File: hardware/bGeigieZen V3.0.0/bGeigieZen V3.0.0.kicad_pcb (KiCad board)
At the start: 2 copper layers, 129.4 x 64.6 mm, 17 parts, among them J1 M5 2x15 pin, J10 QI GND, J11 QI charger Plus, J2 Geiger IRover, J3 GPS, J4 Geiger Safepulse, J5 Extra support header, J6 Grove, J8 QI charger ground, J9 QI Plus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

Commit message: Updated Board V3.0.0
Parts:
- moved J6 3.77 mm to (158.4, 120.2)
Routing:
- net 3.3V: track 140.5 -> 132.3 mm, vias 1 -> 0
- net /SDA: track 49.1 -> 43.4 mm, vias 1 -> 0
- net Net-(BT1--): track 59.1 -> 64.5 mm
- net /SCL: track 50.5 -> 52.4 mm

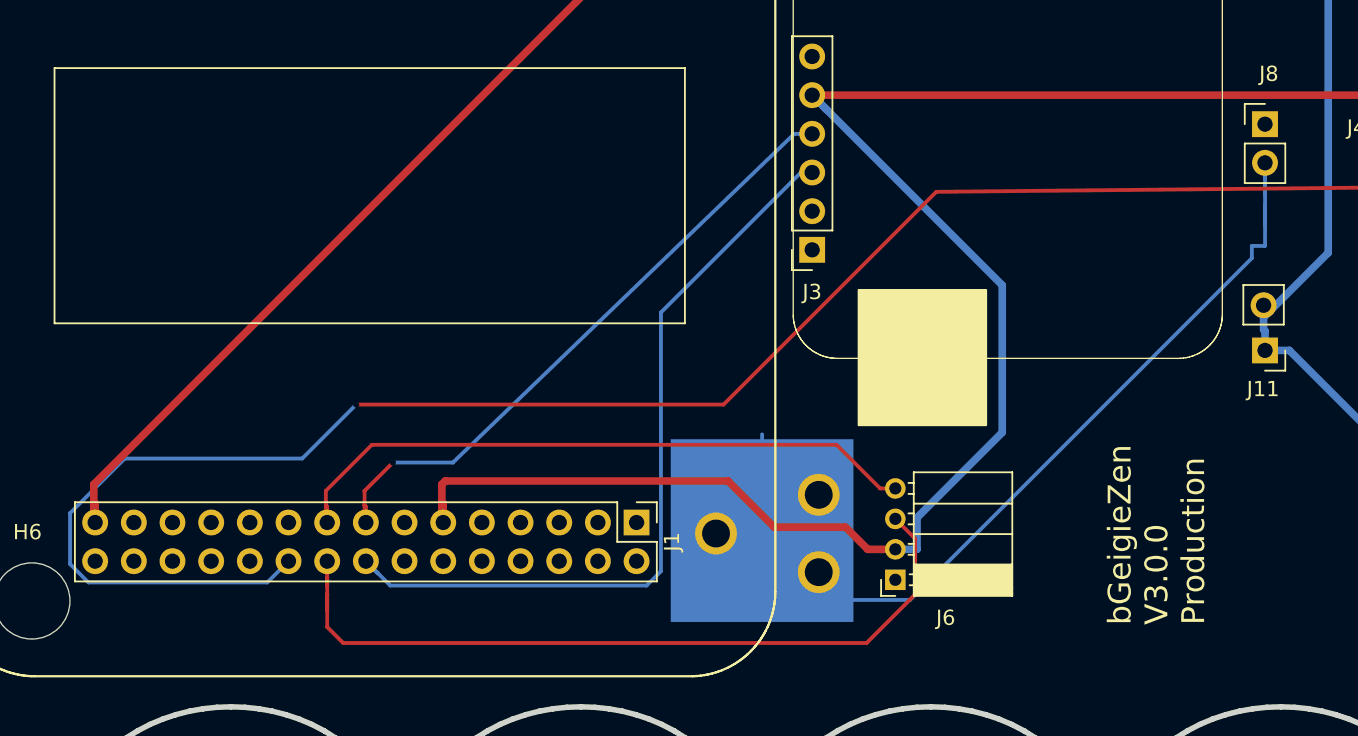
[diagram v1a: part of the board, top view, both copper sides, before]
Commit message: Updated board for IMU and I2C
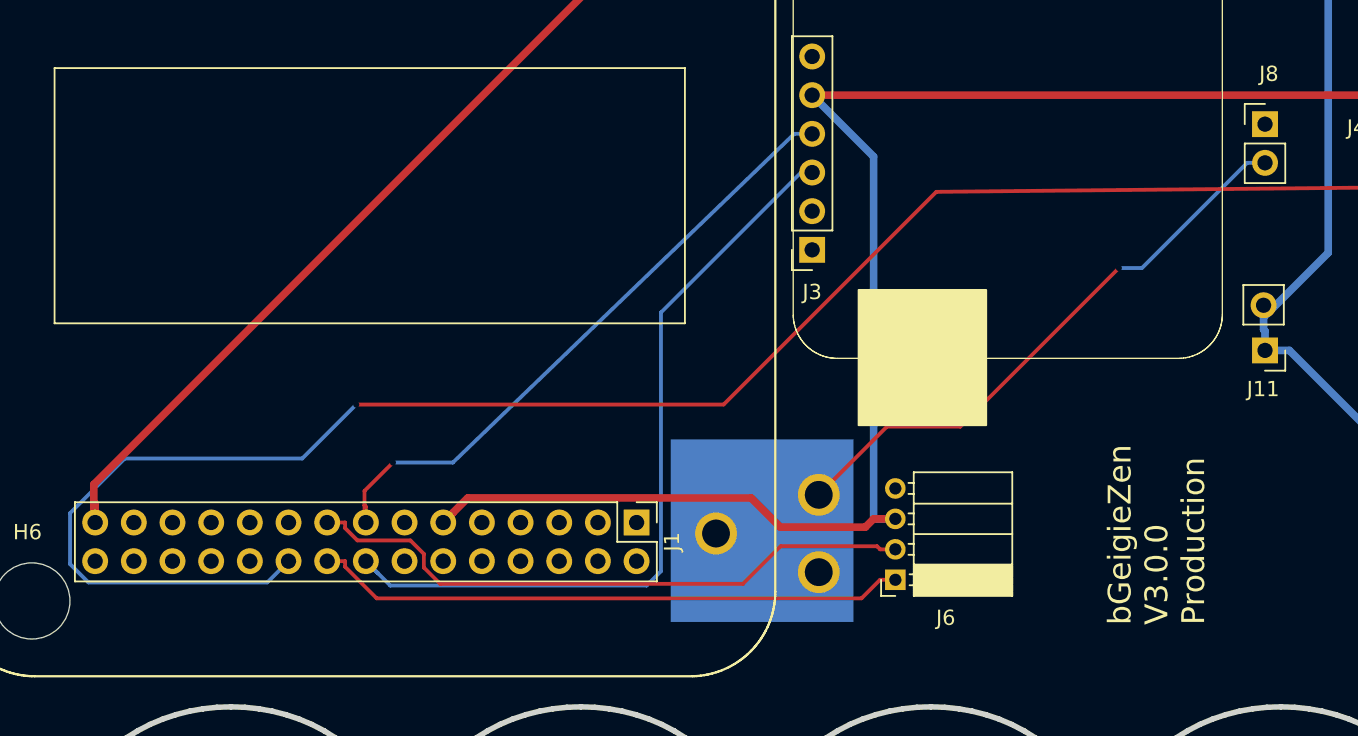
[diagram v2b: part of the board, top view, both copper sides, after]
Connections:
- J6 pad 1: GND -> /SCL
- J6 pad 2: 3.3V -> /SDA
- J6 pad 3: /SCL -> 3.3V
- J6 pad 4: /SDA -> GND
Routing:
- net Net-(BT1--): track 64.5 -> 49.9 mm, vias 0 -> 1
- net /SCL: track 52.4 -> 39.0 mm
- net 3.3V: track 132.3 -> 119.3 mm
- net /SDA: track 43.4 -> 40.8 mm
- net /GIO2 on Core and GIO32 on Core-2: track 138.0 -> 137.1 mm

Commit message: Created n gerbers for V3..0. production boards.
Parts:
- added Logo: LOGO, bGeigieRaku_M5_1015:18650 map, B.Cu at (177.9, 117.3)
- J8: value QI charger ground -> LiPo ground
- moved J6 39.1 mm to (197.1, 114.4), turned to 0 degrees
- moved G back 5.23 mm to (90.9, 99.8)
- moved J3 2.42 mm to (152.9, 96.1)
- moved SW1 1.93 mm to (183.0, 72.6)
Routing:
- net /SCL: track 39.0 -> 81.6 mm
- net /SDA: track 40.8 -> 77.4 mm
- net /GIO2 on Core and GIO32 on Core-2: track 137.1 -> 106.0 mm, vias 1 -> 0
- net 3.3V: track 119.3 -> 131.2 mm
- net /VBATT: track 66.4 -> 67.9 mm
- net /RX2: track 42.4 -> 44.0 mm
- net /TX2: track 51.9 -> 53.1 mm
- net /BAT: track 96.5 -> 95.4 mm
- net Net-(BT1--): track 49.9 -> 49.8 mm, vias 1 -> 0
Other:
- board text added: "-"
- board text added: "IRover"

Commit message: Updated V3.0.0 boards
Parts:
- moved J10 0.94 mm to (209.8, 91.4)
- moved J8 0.94 mm to (182.5, 91.2)
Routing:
- net Net-(J9-Pin_1): track 2.54 -> 0.00 mm
- net Net-(BT1--): track 49.8 -> 48.8 mm

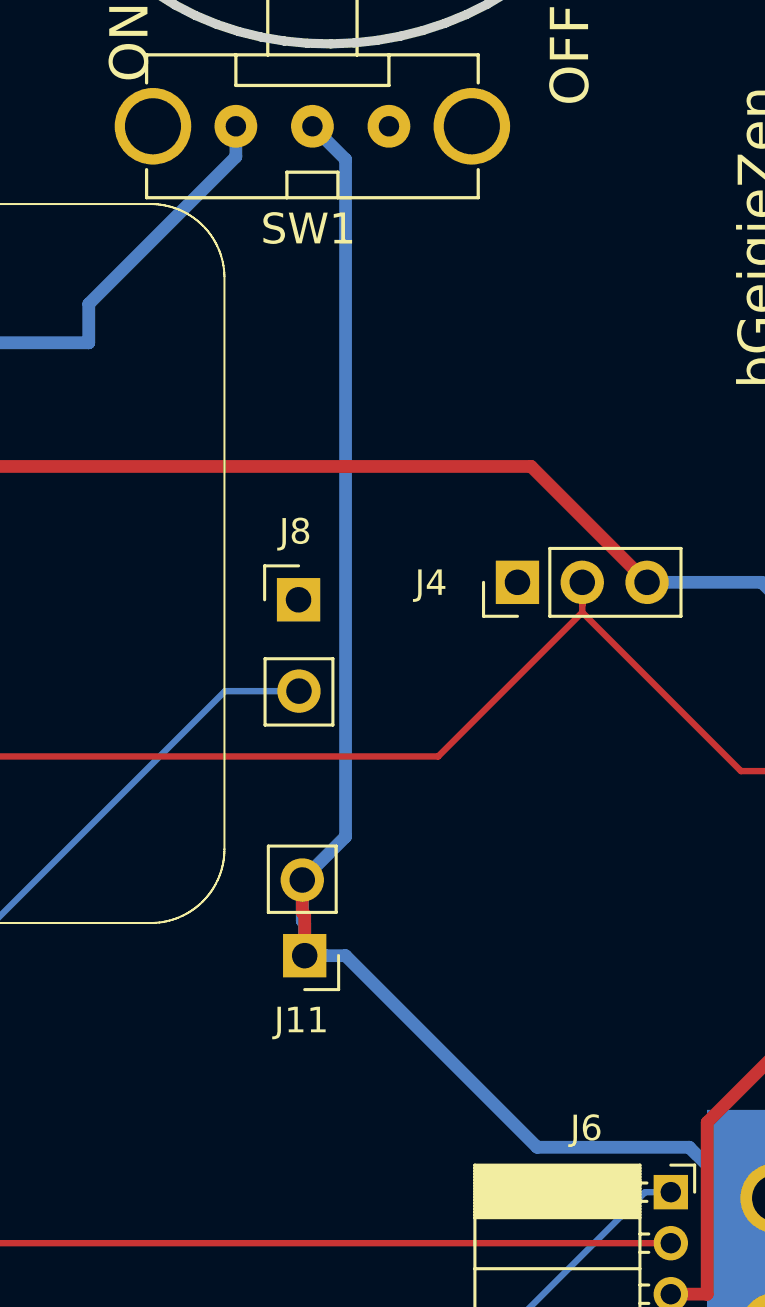
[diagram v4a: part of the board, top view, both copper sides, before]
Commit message: Updated 4056 placement
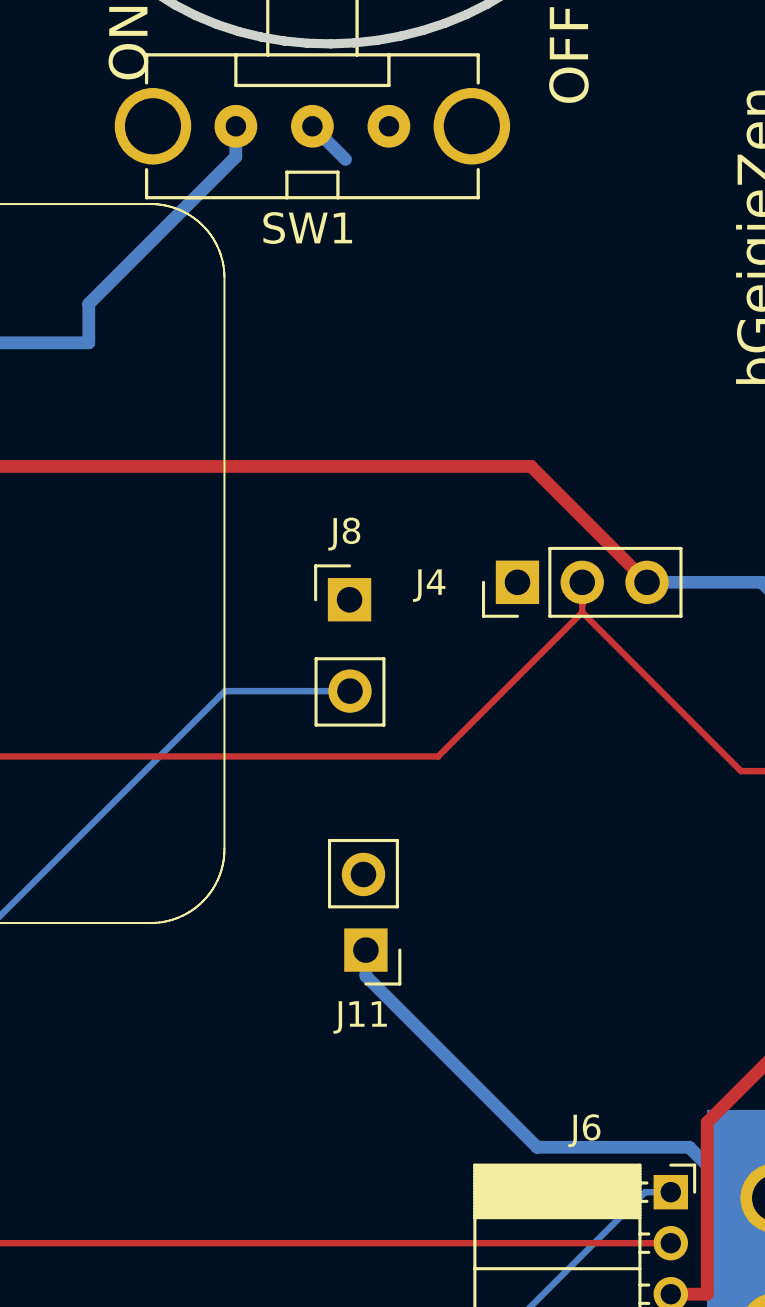
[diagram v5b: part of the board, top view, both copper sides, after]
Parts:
- moved J11 2.41 mm to (185.1, 104.9)
- moved J8 2.00 mm to (184.5, 91.2)
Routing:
- net /VBATT: track 67.9 -> 31.3 mm
- net Net-(BT1--): track 48.8 -> 50.8 mm
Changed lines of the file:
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@@
   )
   (footprint "bGeigieZen:PinHeader_1x02_P2.54mm_Vertical_4056" (layer "F.Cu")
-    (at 182.7276 105.104 180)
+    (at 185.127021 104.8856 180)
     (descr "Through hole straight pin header, 1x02, 2.54mm pitch, single row")
     (tags "Through hole pin header THT 1x02 2.54mm single row")
@@
   )
   (footprint "Connector_PinHeader_2.54mm:PinHeader_1x02_P2.54mm_Vertical" (layer "F.Cu")
-    (at 182.486504 91.153824)
+    (at 184.486504 91.153824)
     (descr "Through hole straight pin header, 1x02, 2.54mm pitch, single row")
     (tags "Through hole pin header THT 1x02 2.54mm single row")
@@
   (segment (start 128.7526 113.2324) (end 128.7526 116.407) (width 0.5) (layer "B.Cu") (net 4))
   (segment (start 152.883 85.9274) (end 152.883 85.9272) (width 0.5) (layer "B.Cu") (net 4))
-  (segment (start 182.632 103.407) (end 182.728 103.502) (width 0.5) (layer "F.Cu") (net 7))
-  (segment (start 182.632 102.138) (end 182.632 102.1385) (width 0.5) (layer "F.Cu") (net 7))
-  (segment (start 182.728 103.502) (end 182.728 104.303) (width 0.5) (layer "F.Cu") (net 7))
-  (segment (start 182.632 102.1385) (end 182.632 103.407) (width 0.5) (layer "F.Cu") (net 7))
+  (segment (start 191.839 112.614) (end 185.127021 105.902021) (width 0.5) (layer "B.Cu") (net 7))
   (segment (start 200.711 117.15) (end 198.78 115.219) (width 0.5) (layer "B.Cu") (net 7))
   (segment (start 207.926 117.15) (end 207.9256 117.15) (width 0.5) (layer "B.Cu") (net 7))
-  (segment (start 182.728 103.836) (end 182.632 103.74) (width 0.5) (layer "B.Cu") (net 7))
-  (segment (start 183.5285 105.104) (end 182.7276 105.104) (width 0.5) (layer "B.Cu") (net 7))
   (segment (start 204.4976 117.15) (end 200.711 117.15) (width 0.5) (layer "B.Cu") (net 7))
-  (segment (start 182.632 102.138) (end 184.3293 100.4407) (width 0.5) (layer "B.Cu") (net 7))
   (segment (start 184.3293 73.8917) (end 183.0296 72.592) (width 0.5) (layer "B.Cu") (net 7))
   (segment (start 198.78 113.592) (end 197.801 112.614) (width 0.5) (layer "B.Cu") (net 7))
-  (segment (start 184.3293 100.4407) (end 184.3293 73.8917) (width 0.5) (layer "B.Cu") (net 7))
-  (segment (start 182.728 105.104) (end 182.728 103.836) (width 0.5) (layer "B.Cu") (net 7))
   (segment (start 198.78 115.219) (end 198.78 113.592) (width 0.5) (layer "B.Cu") (net 7))
-  (segment (start 184.329 105.104) (end 183.5285 105.104) (width 0.5) (layer "B.Cu") (net 7))
   (segment (start 207.9256 117.15) (end 204.4976 117.15) (width 0.5) (layer "B.Cu") (net 7))
   (segment (start 197.801 112.614) (end 191.839 112.614) (width 0.5) (layer "B.Cu") (net 7))
-  (segment (start 183.5285 105.104) (end 182.728 105.104) (width 0.5) (layer "B.Cu") (net 7))
-  (segment (start 182.632 103.74) (end 182.632 102.1385) (width 0.5) (layer "B.Cu") (net 7))
-  (segment (start 182.632 102.138) (end 182.632 102.1385) (width 0.5) (layer "B.Cu") (net 7))
-  (segment (start 191.839 112.614) (end 184.329 105.104) (width 0.5) (layer "B.Cu") (net 7))
+  (segment (start 185.127021 105.902021) (end 185.127021 104.8856) (width 0.5) (layer "B.Cu") (net 7))
   (segment (start 207.108 97.87) (end 199.831 97.87) (width 0.25) (layer "F.Cu") (net 19))
   (segment (start 193.6076 90.7637) (end 193.6076 90.47) (width 0.25) (layer "F.Cu") (net 19))
@@
   (segment (start 149.6976 116.9404) (end 149.698 116.94) (width 0.25) (layer "B.Cu") (net 34))
   (segment (start 153.418 114.59) (end 159.746 114.59) (width 0.25) (layer "B.Cu") (net 34))
-  (segment (start 179.601868 94.734132) (end 182.502811 94.734132) (width 0.25) (layer "B.Cu") (net 34))
   (segment (start 146.67 117.13) (end 149.508 117.13) (width 0.25) (layer "B.Cu") (net 34))
   (segment (start 153.4176 114.5904) (end 153.418 114.59) (width 0.25) (layer "B.Cu") (net 34))
@@
   (segment (start 151.068 117.32) (end 153.4176 119.6696) (width 0.25) (layer "B.Cu") (net 34))
   (segment (start 153.4176 114.5904) (end 153.4176 114.59) (width 0.25) (layer "B.Cu") (net 34))
+  (segment (start 179.601868 94.734132) (end 184.502811 94.734132) (width 0.25) (layer "B.Cu") (net 34))
   (zone (net 1) (net_name "GND") (layers "F&B.Cu") (name "GND") (hatch edge 0.508)
     (connect_pads (clearance 0.508))

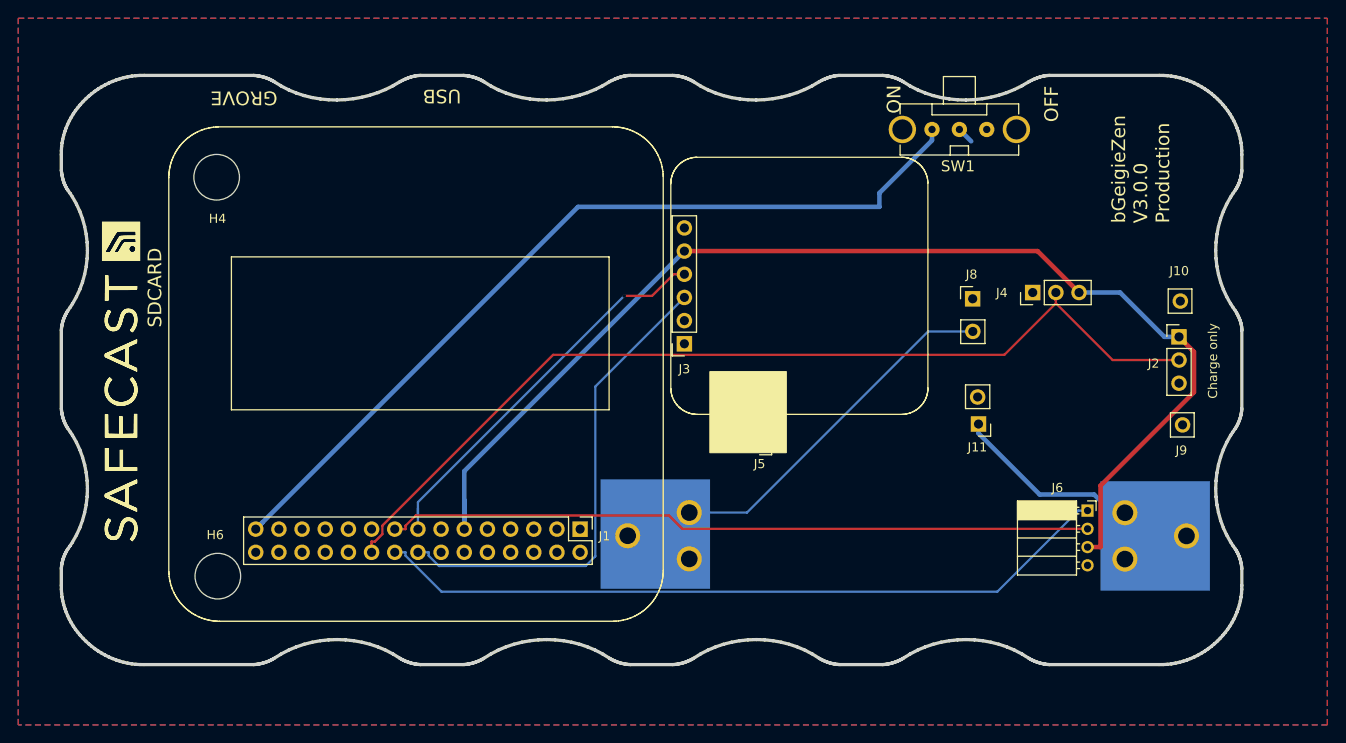
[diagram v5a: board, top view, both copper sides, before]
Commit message: Updated Grove connector on board V3.0.1
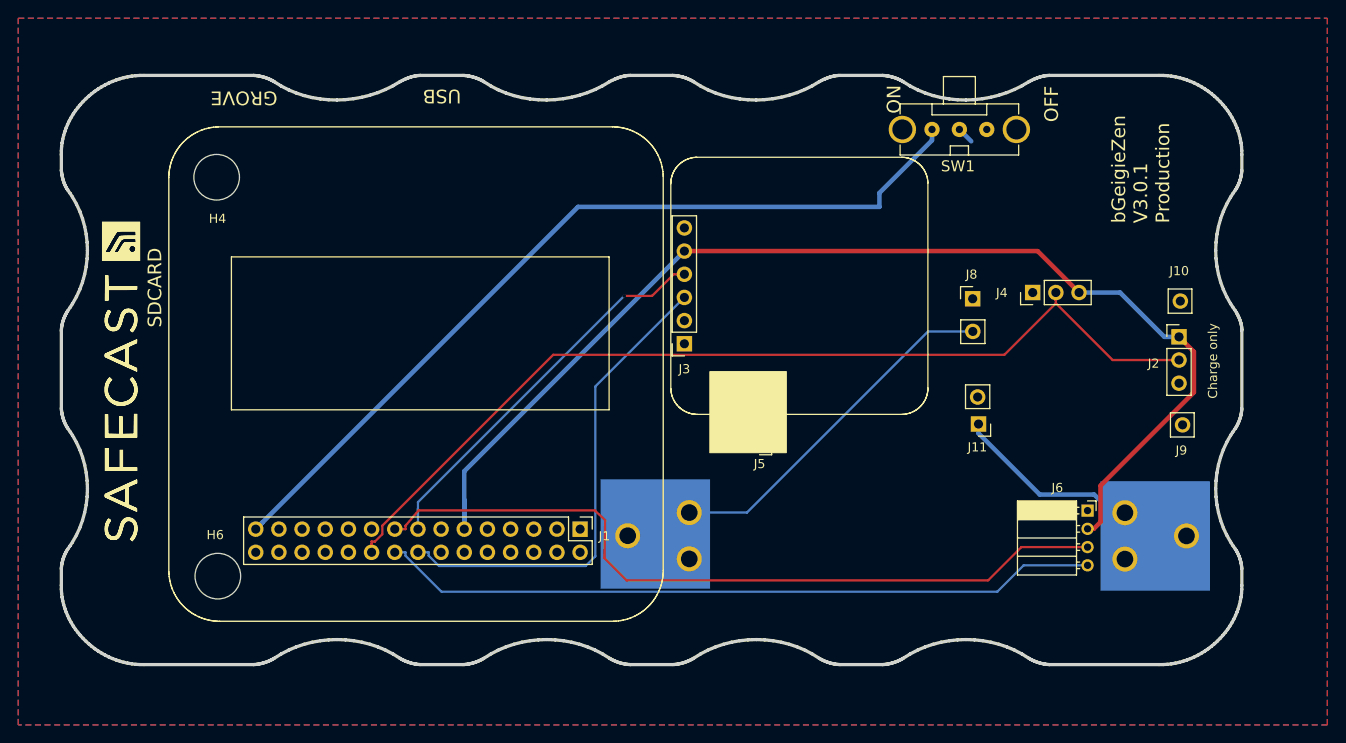
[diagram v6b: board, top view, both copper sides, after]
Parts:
- J8: value LiPo ground -> QI charger ground
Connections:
- BT1 pad BAT Neg: Net-(BT1--) -> (no net)
- J6 pad 1: /SCL -> GND
- J6 pad 2: /SDA -> 3.3V
- J6 pad 3: 3.3V -> /SDA
- J6 pad 4: GND -> /SCL
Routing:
- net /SDA: track 77.4 -> 84.3 mm
- net /SCL: track 81.6 -> 79.1 mm
- net 3.3V: track 131.2 -> 128.7 mm
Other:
- board text added: "bGeigieZen V3.0.1 Production"
- board text removed: "bGeigieZen V3.0.0 Production"
